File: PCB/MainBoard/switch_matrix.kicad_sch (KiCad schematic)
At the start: 136 parts, among them SW10 SW_ctrl, SW11 SW_1, SW12 SW_q, SW13 SW_a, SW14 SW_z, SW15 SW_super, SW16 SW_2, SW17 SW_w, SW18 SW_s, SW19 SW_x, SW2 SW_esc, SW20 SW_alt, SW21 SW_3, SW22 SW_e, SW23 SW_d, SW24 SW_c, SW26 SW_4, SW27 SW_r, SW28 SW_f, SW29 SW_v, SW3 SW_del, SW30 SW_5, SW31 SW_t, SW32 SW_g, SW33 SW_b, SW34 SW_space, SW35 SW_6, SW36 SW_y, SW37 SW_h, SW38 SW_n, SW4 SW_ins, SW40 SW_7, SW41 SW_u, SW42 SW_j, SW43 SW_m, SW44 SW_fn2, SW45 SW_8, SW46 SW_i, SW47 SW_k, SW48 SW_,, SW49 SW_left, SW5 SW_fn1, SW50 SW_9, SW51 SW_o, SW52 SW_l, SW53 SW_., SW54 SW_down, SW55 SW_0, SW56 SW_p, SW57 SW_;, SW58 SW_/, SW59 SW_up, SW6 SW_`, SW60 SW_-, SW61 SW_[, SW62 SW_', SW63 SW_r_shift, SW64 SW_right, SW65 SW_+, SW66 SW_back, SW67 SW_], SW68 SW_\, SW69 SW_enter, SW7 SW_tab, SW8 SW_caps, SW9 SW_shift

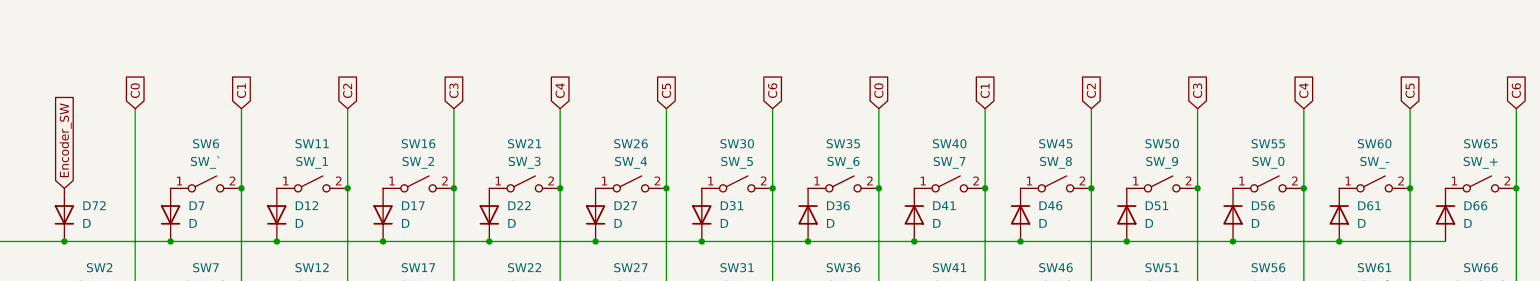
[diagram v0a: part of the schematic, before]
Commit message: Added diodes for the duplex layout
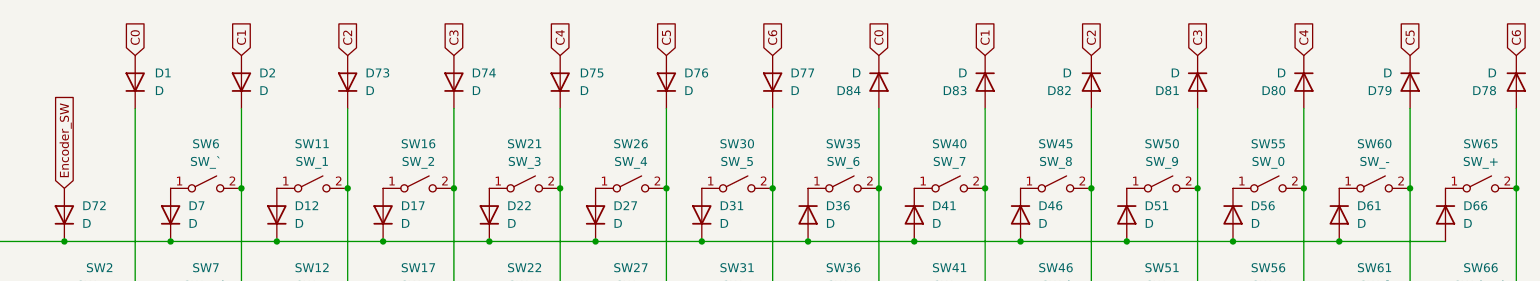
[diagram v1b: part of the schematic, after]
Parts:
- added D1, D2, D73, D74, D75, D76, D77, D78, D79, D80, D81, D82, D83, D84: D, Diode_THT:D_DO-35_SOD27_P7.62mm_Horizontal, symbol Device:D
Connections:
- net C0: now also D1.2 (A), D84.1 (K); no longer SW2.2 (B), SW3.2 (B), SW34.2 (B), SW35.2 (B), SW36.2 (B), SW37.2 (B), SW38.2 (B), SW4.2 (B), SW5.2 (B)
- net C1: now also D2.2 (A), D83.1 (K); no longer SW10.2 (B), SW40.2 (B), SW41.2 (B), SW42.2 (B), SW43.2 (B), SW44.2 (B), SW6.2 (B), SW7.2 (B), SW8.2 (B), SW9.2 (B)
- net C2: now also D73.2 (A), D82.1 (K); no longer SW11.2 (B), SW12.2 (B), SW13.2 (B), SW14.2 (B), SW15.2 (B), SW45.2 (B), SW46.2 (B), SW47.2 (B), SW48.2 (B), SW49.2 (B)
- net C3: now also D74.2 (A), D81.1 (K); no longer SW16.2 (B), SW17.2 (B), SW18.2 (B), SW19.2 (B), SW20.2 (B), SW50.2 (B), SW51.2 (B), SW52.2 (B), SW53.2 (B), SW54.2 (B)
- net C4: now also D75.2 (A), D80.1 (K); no longer SW21.2 (B), SW22.2 (B), SW55.2 (B), SW56.2 (B), SW57.2 (B), SW58.2 (B), SW59.2 (B)
- net C5: now also D76.2 (A), D79.1 (K); no longer SW24.2 (B), SW26.2 (B), SW27.2 (B), SW28.2 (B), SW29.2 (B), SW60.2 (B), SW61.2 (B), SW62.2 (B), SW63.2 (B), SW64.2 (B)
- net C6: now also D77.2 (A), D78.1 (K); no longer SW23.2 (B), SW30.2 (B), SW31.2 (B), SW32.2 (B), SW33.2 (B), SW65.2 (B), SW66.2 (B), SW67.2 (B), SW68.2 (B), SW69.2 (B)
- new net: D78.2 (A), SW65.2 (B), SW66.2 (B), SW67.2 (B), SW68.2 (B), SW69.2 (B)
- new net: D83.2 (A), SW40.2 (B), SW41.2 (B), SW42.2 (B), SW43.2 (B), SW44.2 (B)
- new net: D81.2 (A), SW50.2 (B), SW51.2 (B), SW52.2 (B), SW53.2 (B), SW54.2 (B)
- new net: D73.1 (K), SW11.2 (B), SW12.2 (B), SW13.2 (B), SW14.2 (B), SW15.2 (B)
- new net: D74.1 (K), SW16.2 (B), SW17.2 (B), SW18.2 (B), SW19.2 (B), SW20.2 (B)
- new net: D80.2 (A), SW55.2 (B), SW56.2 (B), SW57.2 (B), SW58.2 (B), SW59.2 (B)
- new net: D84.2 (A), SW34.2 (B), SW35.2 (B), SW36.2 (B), SW37.2 (B), SW38.2 (B)
- new net: D79.2 (A), SW60.2 (B), SW61.2 (B), SW62.2 (B), SW63.2 (B), SW64.2 (B)
- new net: D76.1 (K), SW24.2 (B), SW26.2 (B), SW27.2 (B), SW28.2 (B), SW29.2 (B)
- new net: D2.1 (K), SW10.2 (B), SW6.2 (B), SW7.2 (B), SW8.2 (B), SW9.2 (B)
- new net: D82.2 (A), SW45.2 (B), SW46.2 (B), SW47.2 (B), SW48.2 (B), SW49.2 (B)
- new net: D1.1 (K), SW2.2 (B), SW3.2 (B), SW4.2 (B), SW5.2 (B)
- new net: D77.1 (K), SW23.2 (B), SW30.2 (B), SW31.2 (B), SW32.2 (B), SW33.2 (B)
- new net ExtraSource: D75.1 (K), SW21.2 (B), SW22.2 (B)

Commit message: Updated 3d model
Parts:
- SW10: renamed from SW45; footprint Switch_Keyboard_Hotswap_Kailh:SW_Hotswap_Kailh_MX_1.00u -> PCM_Switch_Keyboard_Hotswap_Kailh:SW_Hotswap_Kailh_MX_1.00u
- SW11: renamed from SW50; footprint Switch_Keyboard_Hotswap_Kailh:SW_Hotswap_Kailh_MX_1.00u -> PCM_Switch_Keyboard_Hotswap_Kailh:SW_Hotswap_Kailh_MX_1.00u
- SW12: renamed from SW55; footprint Switch_Keyboard_Hotswap_Kailh:SW_Hotswap_Kailh_MX_1.00u -> PCM_Switch_Keyboard_Hotswap_Kailh:SW_Hotswap_Kailh_MX_1.00u
- SW13: renamed from SW60; footprint Switch_Keyboard_Hotswap_Kailh:SW_Hotswap_Kailh_MX_1.00u -> PCM_Switch_Keyboard_Hotswap_Kailh:SW_Hotswap_Kailh_MX_1.00u
- SW14: renamed from SW65; footprint Switch_Keyboard_Hotswap_Kailh:SW_Hotswap_Kailh_MX_1.00u -> PCM_Switch_Keyboard_Hotswap_Kailh:SW_Hotswap_Kailh_MX_1.00u
- SW15: renamed from SW2; footprint Switch_Keyboard_Hotswap_Kailh:SW_Hotswap_Kailh_MX_1.00u -> PCM_Switch_Keyboard_Hotswap_Kailh:SW_Hotswap_Kailh_MX_1.00u
- SW16: renamed from SW7; footprint Switch_Keyboard_Hotswap_Kailh:SW_Hotswap_Kailh_MX_1.50u -> PCM_Switch_Keyboard_Hotswap_Kailh:SW_Hotswap_Kailh_MX_1.50u
- SW17: renamed from SW12; footprint Switch_Keyboard_Hotswap_Kailh:SW_Hotswap_Kailh_MX_1.00u -> PCM_Switch_Keyboard_Hotswap_Kailh:SW_Hotswap_Kailh_MX_1.00u
- SW18: renamed from SW17; footprint Switch_Keyboard_Hotswap_Kailh:SW_Hotswap_Kailh_MX_1.00u -> PCM_Switch_Keyboard_Hotswap_Kailh:SW_Hotswap_Kailh_MX_1.00u
- SW19: renamed from SW22; footprint Switch_Keyboard_Hotswap_Kailh:SW_Hotswap_Kailh_MX_1.00u -> PCM_Switch_Keyboard_Hotswap_Kailh:SW_Hotswap_Kailh_MX_1.00u
- SW2: renamed from SW6; footprint Switch_Keyboard_Hotswap_Kailh:SW_Hotswap_Kailh_MX_1.00u -> PCM_Switch_Keyboard_Hotswap_Kailh:SW_Hotswap_Kailh_MX_1.00u
- SW20: renamed from SW27; footprint Switch_Keyboard_Hotswap_Kailh:SW_Hotswap_Kailh_MX_1.00u -> PCM_Switch_Keyboard_Hotswap_Kailh:SW_Hotswap_Kailh_MX_1.00u
- SW21: renamed from SW31; footprint Switch_Keyboard_Hotswap_Kailh:SW_Hotswap_Kailh_MX_1.00u -> PCM_Switch_Keyboard_Hotswap_Kailh:SW_Hotswap_Kailh_MX_1.00u
- SW22: renamed from SW36; footprint Switch_Keyboard_Hotswap_Kailh:SW_Hotswap_Kailh_MX_1.00u -> PCM_Switch_Keyboard_Hotswap_Kailh:SW_Hotswap_Kailh_MX_1.00u
- SW23: renamed from SW41; footprint Switch_Keyboard_Hotswap_Kailh:SW_Hotswap_Kailh_MX_1.00u -> PCM_Switch_Keyboard_Hotswap_Kailh:SW_Hotswap_Kailh_MX_1.00u
- SW24: renamed from SW46; footprint Switch_Keyboard_Hotswap_Kailh:SW_Hotswap_Kailh_MX_1.00u -> PCM_Switch_Keyboard_Hotswap_Kailh:SW_Hotswap_Kailh_MX_1.00u
- SW25: renamed from SW51; footprint Switch_Keyboard_Hotswap_Kailh:SW_Hotswap_Kailh_MX_1.00u -> PCM_Switch_Keyboard_Hotswap_Kailh:SW_Hotswap_Kailh_MX_1.00u
- SW26: renamed from SW56; footprint Switch_Keyboard_Hotswap_Kailh:SW_Hotswap_Kailh_MX_1.00u -> PCM_Switch_Keyboard_Hotswap_Kailh:SW_Hotswap_Kailh_MX_1.00u
- SW27: renamed from SW61; footprint Switch_Keyboard_Hotswap_Kailh:SW_Hotswap_Kailh_MX_1.00u -> PCM_Switch_Keyboard_Hotswap_Kailh:SW_Hotswap_Kailh_MX_1.00u
- SW28: renamed from SW66; footprint Switch_Keyboard_Hotswap_Kailh:SW_Hotswap_Kailh_MX_2.00u -> PCM_Switch_Keyboard_Hotswap_Kailh:SW_Hotswap_Kailh_MX_2.00u
- SW29: renamed from SW3; footprint Switch_Keyboard_Hotswap_Kailh:SW_Hotswap_Kailh_MX_1.00u -> PCM_Switch_Keyboard_Hotswap_Kailh:SW_Hotswap_Kailh_MX_1.00u
- SW3: renamed from SW11; footprint Switch_Keyboard_Hotswap_Kailh:SW_Hotswap_Kailh_MX_1.00u -> PCM_Switch_Keyboard_Hotswap_Kailh:SW_Hotswap_Kailh_MX_1.00u
- SW30: renamed from SW8; footprint Switch_Keyboard_Hotswap_Kailh:SW_Hotswap_Kailh_MX_1.75u -> PCM_Switch_Keyboard_Hotswap_Kailh:SW_Hotswap_Kailh_MX_1.75u
- SW31: renamed from SW13; footprint Switch_Keyboard_Hotswap_Kailh:SW_Hotswap_Kailh_MX_1.00u -> PCM_Switch_Keyboard_Hotswap_Kailh:SW_Hotswap_Kailh_MX_1.00u
- SW32: renamed from SW18; footprint Switch_Keyboard_Hotswap_Kailh:SW_Hotswap_Kailh_MX_1.00u -> PCM_Switch_Keyboard_Hotswap_Kailh:SW_Hotswap_Kailh_MX_1.00u
- SW33: renamed from SW28; footprint Switch_Keyboard_Hotswap_Kailh:SW_Hotswap_Kailh_MX_1.00u -> PCM_Switch_Keyboard_Hotswap_Kailh:SW_Hotswap_Kailh_MX_1.00u
- SW34: renamed from SW32; footprint Switch_Keyboard_Hotswap_Kailh:SW_Hotswap_Kailh_MX_1.00u -> PCM_Switch_Keyboard_Hotswap_Kailh:SW_Hotswap_Kailh_MX_1.00u
- SW35: renamed from SW37; footprint Switch_Keyboard_Hotswap_Kailh:SW_Hotswap_Kailh_MX_1.00u -> PCM_Switch_Keyboard_Hotswap_Kailh:SW_Hotswap_Kailh_MX_1.00u
- SW36: renamed from SW42; footprint Switch_Keyboard_Hotswap_Kailh:SW_Hotswap_Kailh_MX_1.00u -> PCM_Switch_Keyboard_Hotswap_Kailh:SW_Hotswap_Kailh_MX_1.00u
- SW37: renamed from SW47; footprint Switch_Keyboard_Hotswap_Kailh:SW_Hotswap_Kailh_MX_1.00u -> PCM_Switch_Keyboard_Hotswap_Kailh:SW_Hotswap_Kailh_MX_1.00u
- SW38: renamed from SW52; footprint Switch_Keyboard_Hotswap_Kailh:SW_Hotswap_Kailh_MX_1.00u -> PCM_Switch_Keyboard_Hotswap_Kailh:SW_Hotswap_Kailh_MX_1.00u
- SW39: renamed from SW57; footprint Switch_Keyboard_Hotswap_Kailh:SW_Hotswap_Kailh_MX_1.00u -> PCM_Switch_Keyboard_Hotswap_Kailh:SW_Hotswap_Kailh_MX_1.00u
- SW4: renamed from SW16; footprint Switch_Keyboard_Hotswap_Kailh:SW_Hotswap_Kailh_MX_1.00u -> PCM_Switch_Keyboard_Hotswap_Kailh:SW_Hotswap_Kailh_MX_1.00u
- SW40: renamed from SW62; footprint Switch_Keyboard_Hotswap_Kailh:SW_Hotswap_Kailh_MX_1.00u -> PCM_Switch_Keyboard_Hotswap_Kailh:SW_Hotswap_Kailh_MX_1.00u
- SW41: renamed from SW67; footprint Switch_Keyboard_Hotswap_Kailh:SW_Hotswap_Kailh_MX_1.00u -> PCM_Switch_Keyboard_Hotswap_Kailh:SW_Hotswap_Kailh_MX_1.00u
- SW42: renamed from SW4; footprint Switch_Keyboard_Hotswap_Kailh:SW_Hotswap_Kailh_MX_1.00u -> PCM_Switch_Keyboard_Hotswap_Kailh:SW_Hotswap_Kailh_MX_1.00u
- SW43: renamed from SW9; footprint Switch_Keyboard_Hotswap_Kailh:SW_Hotswap_Kailh_MX_2.25u -> PCM_Switch_Keyboard_Hotswap_Kailh:SW_Hotswap_Kailh_MX_2.25u
- SW44: renamed from SW14; footprint Switch_Keyboard_Hotswap_Kailh:SW_Hotswap_Kailh_MX_1.00u -> PCM_Switch_Keyboard_Hotswap_Kailh:SW_Hotswap_Kailh_MX_1.00u
- SW45: renamed from SW19; footprint Switch_Keyboard_Hotswap_Kailh:SW_Hotswap_Kailh_MX_1.00u -> PCM_Switch_Keyboard_Hotswap_Kailh:SW_Hotswap_Kailh_MX_1.00u
- SW46: renamed from SW29; footprint Switch_Keyboard_Hotswap_Kailh:SW_Hotswap_Kailh_MX_1.00u -> PCM_Switch_Keyboard_Hotswap_Kailh:SW_Hotswap_Kailh_MX_1.00u
- SW47: renamed from SW33; footprint Switch_Keyboard_Hotswap_Kailh:SW_Hotswap_Kailh_MX_1.00u -> PCM_Switch_Keyboard_Hotswap_Kailh:SW_Hotswap_Kailh_MX_1.00u
- SW48: renamed from SW38; footprint Switch_Keyboard_Hotswap_Kailh:SW_Hotswap_Kailh_MX_1.00u -> PCM_Switch_Keyboard_Hotswap_Kailh:SW_Hotswap_Kailh_MX_1.00u
- SW49: renamed from SW43; footprint Switch_Keyboard_Hotswap_Kailh:SW_Hotswap_Kailh_MX_1.00u -> PCM_Switch_Keyboard_Hotswap_Kailh:SW_Hotswap_Kailh_MX_1.00u
- SW5: renamed from SW21; footprint Switch_Keyboard_Hotswap_Kailh:SW_Hotswap_Kailh_MX_1.00u -> PCM_Switch_Keyboard_Hotswap_Kailh:SW_Hotswap_Kailh_MX_1.00u
- SW50: renamed from SW48; footprint Switch_Keyboard_Hotswap_Kailh:SW_Hotswap_Kailh_MX_1.00u -> PCM_Switch_Keyboard_Hotswap_Kailh:SW_Hotswap_Kailh_MX_1.00u
- SW51: renamed from SW53; footprint Switch_Keyboard_Hotswap_Kailh:SW_Hotswap_Kailh_MX_1.00u -> PCM_Switch_Keyboard_Hotswap_Kailh:SW_Hotswap_Kailh_MX_1.00u
- SW52: renamed from SW58; footprint Switch_Keyboard_Hotswap_Kailh:SW_Hotswap_Kailh_MX_1.00u -> PCM_Switch_Keyboard_Hotswap_Kailh:SW_Hotswap_Kailh_MX_1.00u
- SW53: renamed from SW63; footprint Switch_Keyboard_Hotswap_Kailh:SW_Hotswap_Kailh_MX_2.75u -> PCM_Switch_Keyboard_Hotswap_Kailh:SW_Hotswap_Kailh_MX_2.75u
- SW54: renamed from SW68; footprint Switch_Keyboard_Hotswap_Kailh:SW_Hotswap_Kailh_MX_1.50u -> PCM_Switch_Keyboard_Hotswap_Kailh:SW_Hotswap_Kailh_MX_1.50u
- SW55: renamed from SW24; footprint Switch_Keyboard_Hotswap_Kailh:SW_Hotswap_Kailh_MX_1.00u -> PCM_Switch_Keyboard_Hotswap_Kailh:SW_Hotswap_Kailh_MX_1.00u
- SW56: renamed from SW5; footprint Switch_Keyboard_Hotswap_Kailh:SW_Hotswap_Kailh_MX_1.00u -> PCM_Switch_Keyboard_Hotswap_Kailh:SW_Hotswap_Kailh_MX_1.00u
- SW57: renamed from SW10; footprint Switch_Keyboard_Hotswap_Kailh:SW_Hotswap_Kailh_MX_1.25u -> PCM_Switch_Keyboard_Hotswap_Kailh:SW_Hotswap_Kailh_MX_1.25u
- SW58: renamed from SW15; footprint Switch_Keyboard_Hotswap_Kailh:SW_Hotswap_Kailh_MX_1.25u -> PCM_Switch_Keyboard_Hotswap_Kailh:SW_Hotswap_Kailh_MX_1.25u
- SW59: renamed from SW20; footprint Switch_Keyboard_Hotswap_Kailh:SW_Hotswap_Kailh_MX_1.25u -> PCM_Switch_Keyboard_Hotswap_Kailh:SW_Hotswap_Kailh_MX_1.25u
- SW6: renamed from SW26; footprint Switch_Keyboard_Hotswap_Kailh:SW_Hotswap_Kailh_MX_1.00u -> PCM_Switch_Keyboard_Hotswap_Kailh:SW_Hotswap_Kailh_MX_1.00u
- SW60: renamed from SW23; footprint Switch_Keyboard_Hotswap_Kailh:SW_Hotswap_Kailh_MX_1.00u -> PCM_Switch_Keyboard_Hotswap_Kailh:SW_Hotswap_Kailh_MX_1.00u
- SW61: renamed from SW34; footprint Switch_Keyboard_Hotswap_Kailh:SW_Hotswap_Kailh_MX_6.25u -> PCM_Switch_Keyboard_Hotswap_Kailh:SW_Hotswap_Kailh_MX_6.25u
- SW62: renamed from SW44; footprint Switch_Keyboard_Hotswap_Kailh:SW_Hotswap_Kailh_MX_1.00u -> PCM_Switch_Keyboard_Hotswap_Kailh:SW_Hotswap_Kailh_MX_1.00u
- SW63: renamed from SW49; footprint Switch_Keyboard_Hotswap_Kailh:SW_Hotswap_Kailh_MX_1.00u -> PCM_Switch_Keyboard_Hotswap_Kailh:SW_Hotswap_Kailh_MX_1.00u
- SW64: renamed from SW54; footprint Switch_Keyboard_Hotswap_Kailh:SW_Hotswap_Kailh_MX_1.00u -> PCM_Switch_Keyboard_Hotswap_Kailh:SW_Hotswap_Kailh_MX_1.00u
- SW65: renamed from SW59; footprint Switch_Keyboard_Hotswap_Kailh:SW_Hotswap_Kailh_MX_1.00u -> PCM_Switch_Keyboard_Hotswap_Kailh:SW_Hotswap_Kailh_MX_1.00u
- SW66: renamed from SW64; footprint Switch_Keyboard_Hotswap_Kailh:SW_Hotswap_Kailh_MX_1.00u -> PCM_Switch_Keyboard_Hotswap_Kailh:SW_Hotswap_Kailh_MX_1.00u
- SW67: renamed from SW69; footprint Switch_Keyboard_Hotswap_Kailh:SW_Hotswap_Kailh_MX_2.25u -> PCM_Switch_Keyboard_Hotswap_Kailh:SW_Hotswap_Kailh_MX_2.25u
- SW7: renamed from SW30; footprint Switch_Keyboard_Hotswap_Kailh:SW_Hotswap_Kailh_MX_1.00u -> PCM_Switch_Keyboard_Hotswap_Kailh:SW_Hotswap_Kailh_MX_1.00u
- SW8: renamed from SW35; footprint Switch_Keyboard_Hotswap_Kailh:SW_Hotswap_Kailh_MX_1.00u -> PCM_Switch_Keyboard_Hotswap_Kailh:SW_Hotswap_Kailh_MX_1.00u
- SW9: renamed from SW40; footprint Switch_Keyboard_Hotswap_Kailh:SW_Hotswap_Kailh_MX_1.00u -> PCM_Switch_Keyboard_Hotswap_Kailh:SW_Hotswap_Kailh_MX_1.00u
- renumbered D82 to D10, D81 to D11, D80 to D12, D79 to D13, D78 to D14, D72 to D15, D7 to D16, D12 to D17, D17 to D18, D22 to D19, D27 to D20, D31 to D21, D36 to D22, D41 to D23, D46 to D24, D51 to D25, D56 to D26, D61 to D27, D66 to D28, D3 to D29, D73 to D3, D8 to D30, D13 to D31, D18 to D32, D23 to D33, D28 to D34, D32 to D35, D37 to D36, D42 to D37, D47 to D38, D52 to D39, D74 to D4, D57 to D40, D62 to D41, D67 to D42, D4 to D43, D9 to D44, D14 to D45, D19 to D46, D40 to D47, D29 to D48, D33 to D49, D75 to D5, D38 to D50, D43 to D51, D48 to D52, D58 to D54, D63 to D55, D68 to D56, D5 to D57, D10 to D58, D15 to D59, D76 to D6, D20 to D60, D71 to D61, D30 to D62, D34 to D63, D39 to D64, D44 to D65, D49 to D66, D54 to D67, D59 to D68, D64 to D69, D77 to D7, D69 to D70, D6 to D71, D11 to D72, D16 to D73, D21 to D74, D26 to D75, D25 to D76, D24 to D77, D35 to D78, D45 to D79, D84 to D8, D50 to D80, D55 to D81, D60 to D82, D65 to D83, D70 to D84, D83 to D9
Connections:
- net Encoder_SW_2: now reaches D1.1 (K), SW15.2 (B), SW29.2 (B), SW42.2 (B), SW56.2 (B)
- net Encoder_SW renamed Encoder_SW_1

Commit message: Layout settled
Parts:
- renumbered SW9 to SW10, SW10 to SW11, SW11 to SW12, SW12 to SW13, SW13 to SW14, SW14 to SW15, SW15 to SW16, SW16 to SW17, SW17 to SW18, SW18 to SW19, SW19 to SW20, SW20 to SW21, SW21 to SW22, SW22 to SW23, SW23 to SW24, SW24 to SW25, SW25 to SW26, SW26 to SW27, SW27 to SW28, SW28 to SW29, SW2 to SW3, SW29 to SW30, SW30 to SW31, SW31 to SW32, SW32 to SW33, SW33 to SW34, SW34 to SW35, SW35 to SW36, SW36 to SW37, SW37 to SW38, SW38 to SW39, SW3 to SW4, SW39 to SW40, SW40 to SW41, SW41 to SW42, SW42 to SW43, SW43 to SW44, SW44 to SW45, SW45 to SW46, SW46 to SW47, SW47 to SW48, SW48 to SW49, SW4 to SW5, SW49 to SW50, SW50 to SW51, SW51 to SW52, SW52 to SW53, SW53 to SW54, SW54 to SW55, SW55 to SW56, SW56 to SW57, SW57 to SW58, SW58 to SW59, SW5 to SW6, SW59 to SW60, SW60 to SW61, SW61 to SW62, SW62 to SW63, SW63 to SW64, SW64 to SW65, SW65 to SW66, SW66 to SW67, SW67 to SW68, SW6 to SW7, SW7 to SW8, SW8 to SW9

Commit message: Whatever
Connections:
- net at D76.2 (A): now also SW56.1 (A)
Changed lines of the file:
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@@
   (junction (at 54.61 140.97) (diameter 0) (color 0 0 0 0)
   )
-  (junction (at 140.97 115.57) (diameter 0) (color 0 0 0 0)
-  )
   (junction (at 186.69 97.79) (diameter 0) (color 0 0 0 0)
   )
@@
   (junction (at 171.45 97.79) (diameter 0) (color 0 0 0 0)
   )
+  (junction (at 140.97 115.57) (diameter 0) (color 0 0 0 0)
+  )
   (junction (at 100.33 105.41) (diameter 0) (color 0 0 0 0)
   )
@@
   (junction (at 54.61 105.41) (diameter 0) (color 0 0 0 0)
   )
-  (junction (at 140.97 133.2992) (diameter 0) (color 0 0 0 0)
-  )
   (junction (at 85.09 140.97) (diameter 0) (color 0 0 0 0)
   )
@@
     (stroke (width 0) (type default))
   )
+  (wire (pts (xy 140.97 115.57) (xy 140.97 133.35))
+    (stroke (width 0) (type default))
+  )
   (wire (pts (xy 207.01 87.63) (xy 222.25 87.63))
     (stroke (width 0) (type default))
@@
     (stroke (width 0) (type default))
   )
-  (wire (pts (xy 140.97 133.2992) (xy 140.97 133.35))
-    (stroke (width 0) (type default))
-  )
   (wire (pts (xy 217.17 115.57) (xy 217.17 133.35))
     (stroke (width 0) (type default))
@@
     (stroke (width 0) (type default))
   )
-  (wire (pts (xy 140.97 115.57) (xy 140.97 133.2992))
-    (stroke (width 0) (type default))
-  )
   (wire (pts (xy 115.57 69.85) (xy 130.81 69.85))
     (stroke (width 0) (type default))
@@
     )
   )
-  (symbol (lib_id "Switch:SW_SPST") (at 135.89 133.2992 0) (unit 1)
+  (symbol (lib_id "Switch:SW_SPST") (at 135.89 133.35 0) (unit 1)
     (in_bom yes) (on_board yes) (dnp no) (fields_autoplaced)
-    (property "Reference" "SW56" (at 135.89 126.9492 0)
+    (property "Reference" "SW56" (at 135.89 127 0)
       (effects (font (size 1.27 1.27)))
     )
-    (property "Value" "SW_c" (at 135.89 129.4892 0)
+    (property "Value" "SW_c" (at 135.89 129.54 0)
       (effects (font (size 1.27 1.27)))
     )
-    (property "Footprint" "PCM_Switch_Keyboard_Hotswap_Kailh:SW_Hotswap_Kailh_MX_1.00u" (at 135.89 133.2992 0)
+    (property "Footprint" "PCM_Switch_Keyboard_Hotswap_Kailh:SW_Hotswap_Kailh_MX_1.00u" (at 135.89 133.35 0)
       (effects (font (size 1.27 1.27)) hide)
     )
-    (property "Datasheet" "~" (at 135.89 133.2992 0)
+    (property "Datasheet" "~" (at 135.89 133.35 0)
       (effects (font (size 1.27 1.27)) hide)
     )

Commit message: Custom diode footprint with proper silkscreen
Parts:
- D1, D10, D11, D12, D13, D14, D15, D16, D17, D18, D19, D2, D20, D21, D22, D23, D24, D25, D26, D27, D28, D29, D3, D30, D31, D32, D33, D34, D35, D36, D37, D38, D39, D4, D40, D41, D42, D43, D44, D45, D46, D47, D48, D49, D5, D50, D51, D52, D53, D54, D55, D56, D57, D58, D59, D6, D60, D61, D62, D63, D64, D65, D66, D67, D68, D69, D7, D70, D71, D72, D73, D74, D75, D76, D77, D78, D79, D8, D80, D81, D82, D83, D84, D9: footprint Diode_THT:D_DO-35_SOD27_P7.62mm_Horizontal -> Diode_THT_Custom:D_DO-35_SOD27_P7.62mm_Horizontal

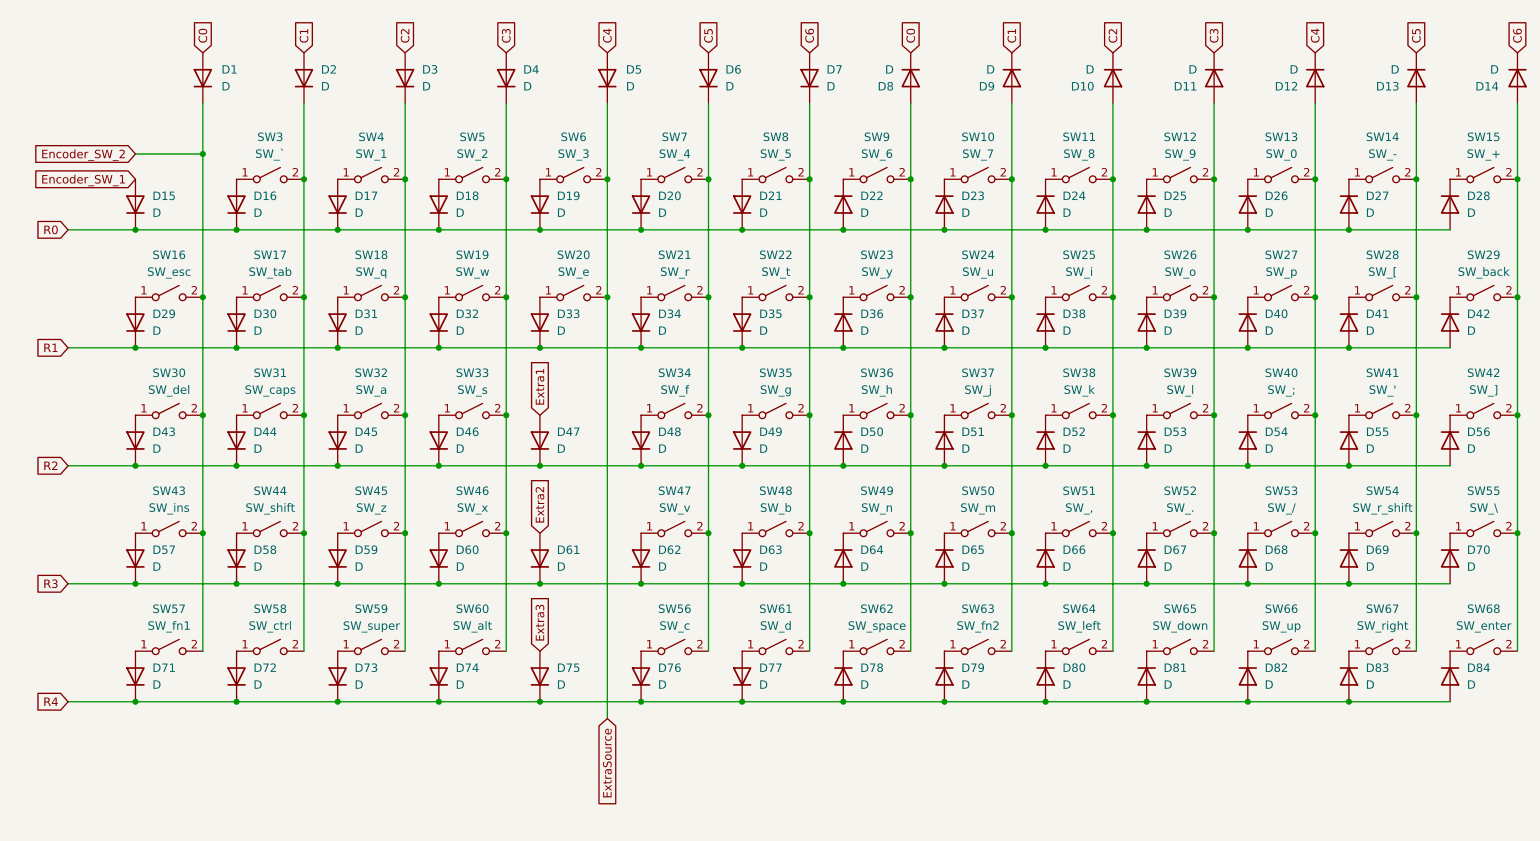
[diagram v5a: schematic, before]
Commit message: Updated the bottom connector, and replotted the files
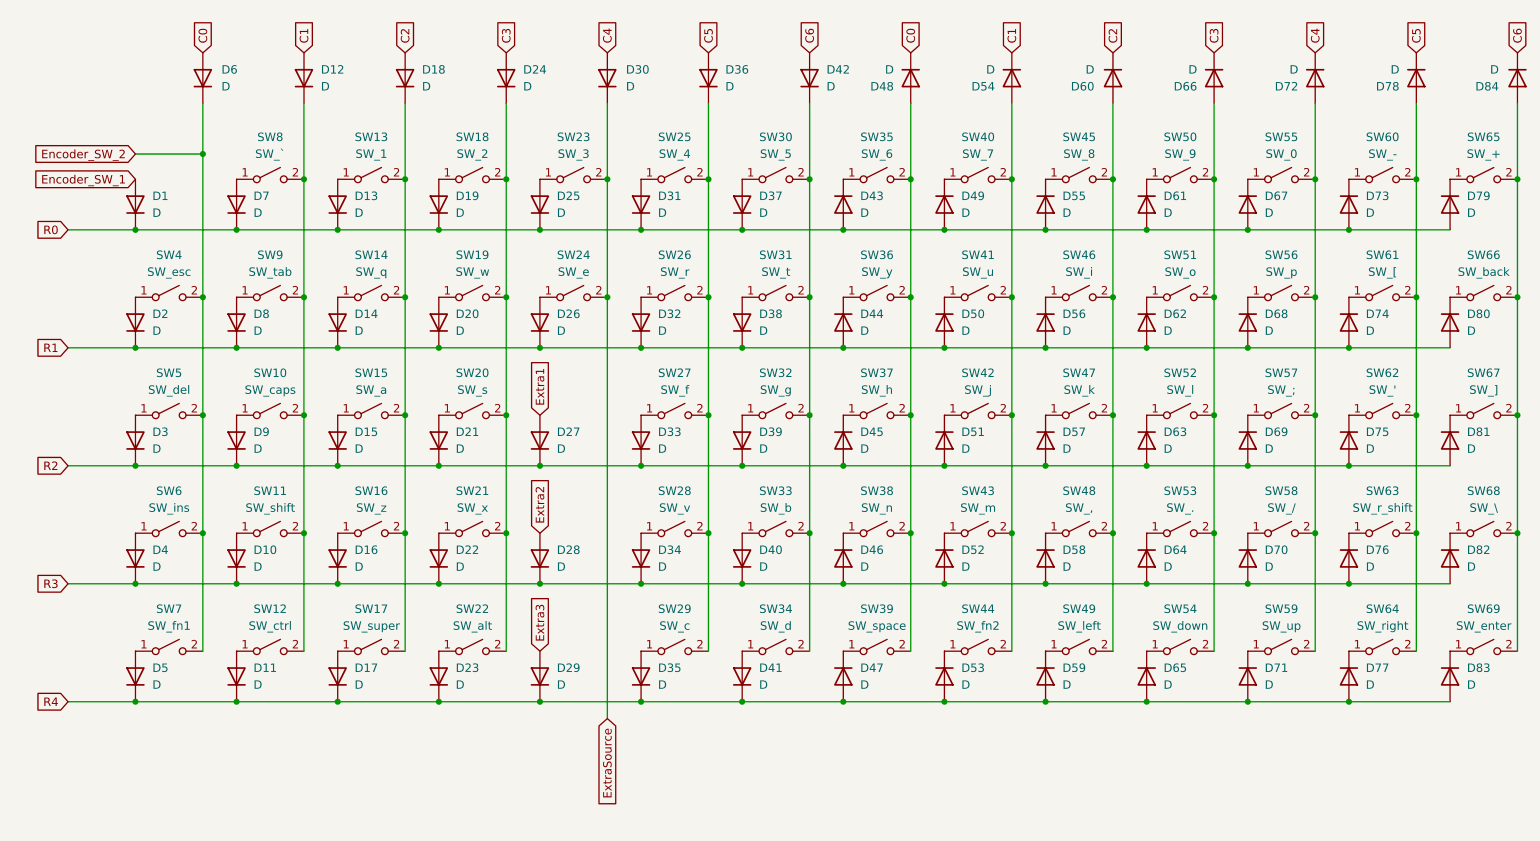
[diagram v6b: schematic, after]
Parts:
- renumbered D15 to D1, D58 to D10, D72 to D11, D2 to D12, D17 to D13, D31 to D14, D45 to D15, D59 to D16, D73 to D17, D3 to D18, D18 to D19, D29 to D2, D32 to D20, D46 to D21, D60 to D22, D74 to D23, D4 to D24, D19 to D25, D33 to D26, D47 to D27, D61 to D28, D75 to D29, D43 to D3, D5 to D30, D20 to D31, D34 to D32, D48 to D33, D62 to D34, D76 to D35, D6 to D36, D21 to D37, D35 to D38, D49 to D39, D57 to D4, D63 to D40, D77 to D41, D7 to D42, D22 to D43, D36 to D44, D50 to D45, D64 to D46, D78 to D47, D8 to D48, D23 to D49, D71 to D5, D37 to D50, D65 to D52, D79 to D53, D9 to D54, D24 to D55, D38 to D56, D52 to D57, D66 to D58, D80 to D59, D1 to D6, D10 to D60, D25 to D61, D39 to D62, D53 to D63, D67 to D64, D81 to D65, D11 to D66, D26 to D67, D40 to D68, D54 to D69, D16 to D7, D68 to D70, D82 to D71, D12 to D72, D27 to D73, D41 to D74, D55 to D75, D69 to D76, D83 to D77, D13 to D78, D28 to D79, D30 to D8, D42 to D80, D56 to D81, D70 to D82, D84 to D83, D14 to D84, D44 to D9, SW31 to SW10, SW44 to SW11, SW58 to SW12, SW4 to SW13, SW18 to SW14, SW32 to SW15, SW45 to SW16, SW59 to SW17, SW5 to SW18, SW33 to SW20, SW46 to SW21, SW60 to SW22, SW6 to SW23, SW20 to SW24, SW7 to SW25, SW21 to SW26, SW34 to SW27, SW47 to SW28, SW56 to SW29, SW8 to SW30, SW22 to SW31, SW35 to SW32, SW48 to SW33, SW61 to SW34, SW9 to SW35, SW23 to SW36, SW36 to SW37, SW49 to SW38, SW62 to SW39, SW16 to SW4, SW10 to SW40, SW24 to SW41, SW37 to SW42, SW50 to SW43, SW63 to SW44, SW11 to SW45, SW25 to SW46, SW38 to SW47, SW51 to SW48, SW64 to SW49, SW30 to SW5, SW12 to SW50, SW26 to SW51, SW39 to SW52, SW52 to SW53, SW65 to SW54, SW13 to SW55, SW27 to SW56, SW40 to SW57, SW53 to SW58, SW66 to SW59, SW43 to SW6, SW14 to SW60, SW28 to SW61, SW41 to SW62, SW54 to SW63, SW67 to SW64, SW15 to SW65, SW29 to SW66, SW42 to SW67, SW55 to SW68, SW68 to SW69, SW57 to SW7, SW3 to SW8, SW17 to SW9

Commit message: Fixed pick and place center for switch footprint
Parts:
- SW10: footprint PCM_Switch_Keyboard_Hotswap_Kailh:SW_Hotswap_Kailh_MX_1.75u -> HotswapFix:SW_Hotswap_Kailh_MX_1.75u
- SW11, SW69: footprint PCM_Switch_Keyboard_Hotswap_Kailh:SW_Hotswap_Kailh_MX_2.25u -> HotswapFix:SW_Hotswap_Kailh_MX_2.25u
- SW12, SW17, SW22: footprint PCM_Switch_Keyboard_Hotswap_Kailh:SW_Hotswap_Kailh_MX_1.25u -> HotswapFix:SW_Hotswap_Kailh_MX_1.25u
- SW13, SW14, SW15, SW16, SW18, SW19, SW20, SW21, SW23, SW24, SW25, SW26, SW27, SW28, SW29, SW30, SW31, SW32, SW33, SW34, SW35, SW36, SW37, SW38, SW4, SW40, SW41, SW42, SW43, SW44, SW45, SW46, SW47, SW48, SW49, SW5, SW50, SW51, SW52, SW53, SW54, SW55, SW56, SW57, SW58, SW59, SW6, SW60, SW61, SW62, SW64, SW65, SW67, SW7, SW8: footprint PCM_Switch_Keyboard_Hotswap_Kailh:SW_Hotswap_Kailh_MX_1.00u -> HotswapFix:SW_Hotswap_Kailh_MX_1.00u
- SW39: footprint PCM_Switch_Keyboard_Hotswap_Kailh:SW_Hotswap_Kailh_MX_6.25u -> HotswapFix:SW_Hotswap_Kailh_MX_6.25u
- SW63: footprint PCM_Switch_Keyboard_Hotswap_Kailh:SW_Hotswap_Kailh_MX_2.75u -> HotswapFix:SW_Hotswap_Kailh_MX_2.75u
- SW66: footprint PCM_Switch_Keyboard_Hotswap_Kailh:SW_Hotswap_Kailh_MX_2.00u -> HotswapFix:SW_Hotswap_Kailh_MX_2.00u
- SW68, SW9: footprint PCM_Switch_Keyboard_Hotswap_Kailh:SW_Hotswap_Kailh_MX_1.50u -> HotswapFix:SW_Hotswap_Kailh_MX_1.50u
